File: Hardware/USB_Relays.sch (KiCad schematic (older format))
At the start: 0 parts

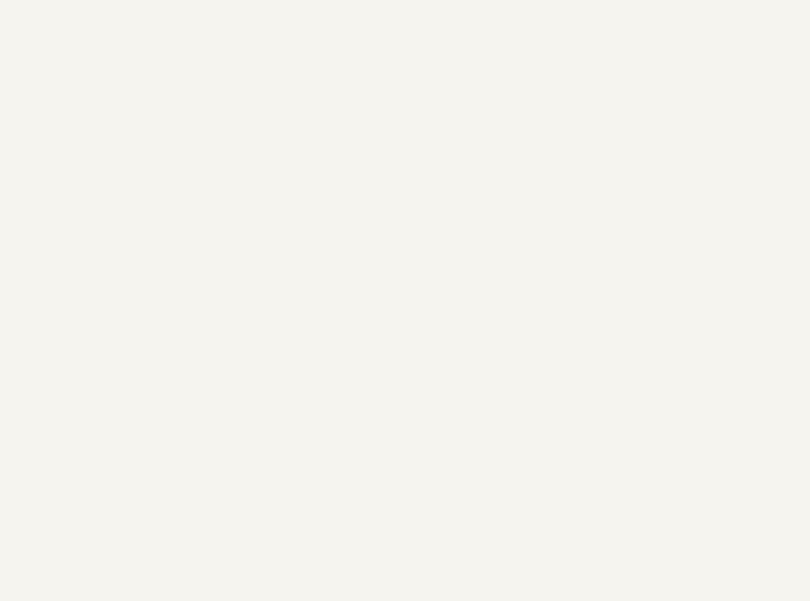
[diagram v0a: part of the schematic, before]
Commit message: [Hardware] Added terminal 3D models.
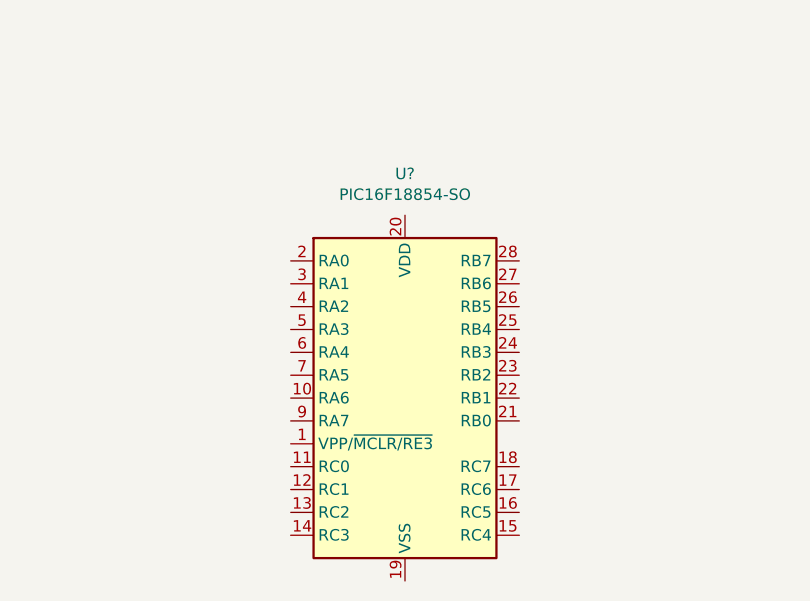
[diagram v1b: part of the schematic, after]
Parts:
- added U?: PIC16F18854-SO, Package_SO:SOIC-28W_7.5x17.9mm_P1.27mm, symbol MCU_Microchip_PIC16:PIC16F18854-SO
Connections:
- new net: U?.19 (VSS), U?.8 (VSS)
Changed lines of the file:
@@
 F1 "USB.sch" 50
 $EndSheet
+$Comp
+L MCU_Microchip_PIC16:PIC16F18854-SO U?
+U 1 1 6170521F
+P 3850 5250
+F 0 "U?" H 3850 6231 50  0000 C CNN
+F 1 "PIC16F18854-SO" H 3850 6140 50  0000 C CNN
+F 2 "Package_SO:SOIC-28W_7.5x17.9mm_P1.27mm" H 3850 4150 50  0001 C CNN
+F 3 "http://ww1.microchip.com/downloads/en/DeviceDoc/PIC16(L)F18854%20Data%20Sheet_DS40001826C.pdf" H 4150 4650 50  0001 C CNN
+	1    3850 5250
+	1    0    0    -1
+$EndComp
 $EndSCHEMATC

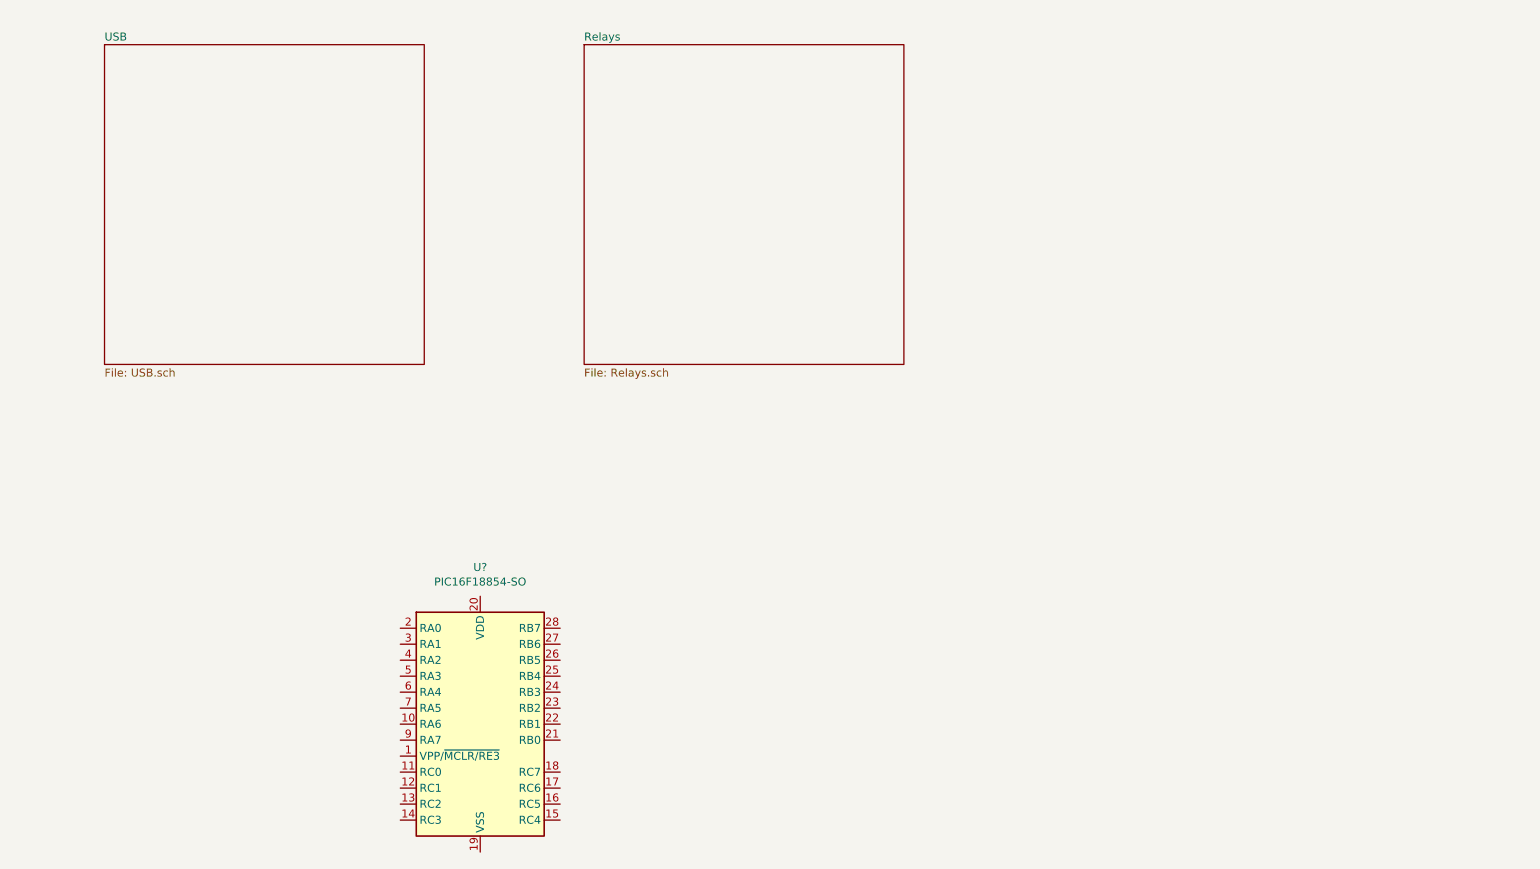
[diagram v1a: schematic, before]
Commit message: [Hardware] Added microcontroller-related schematic.
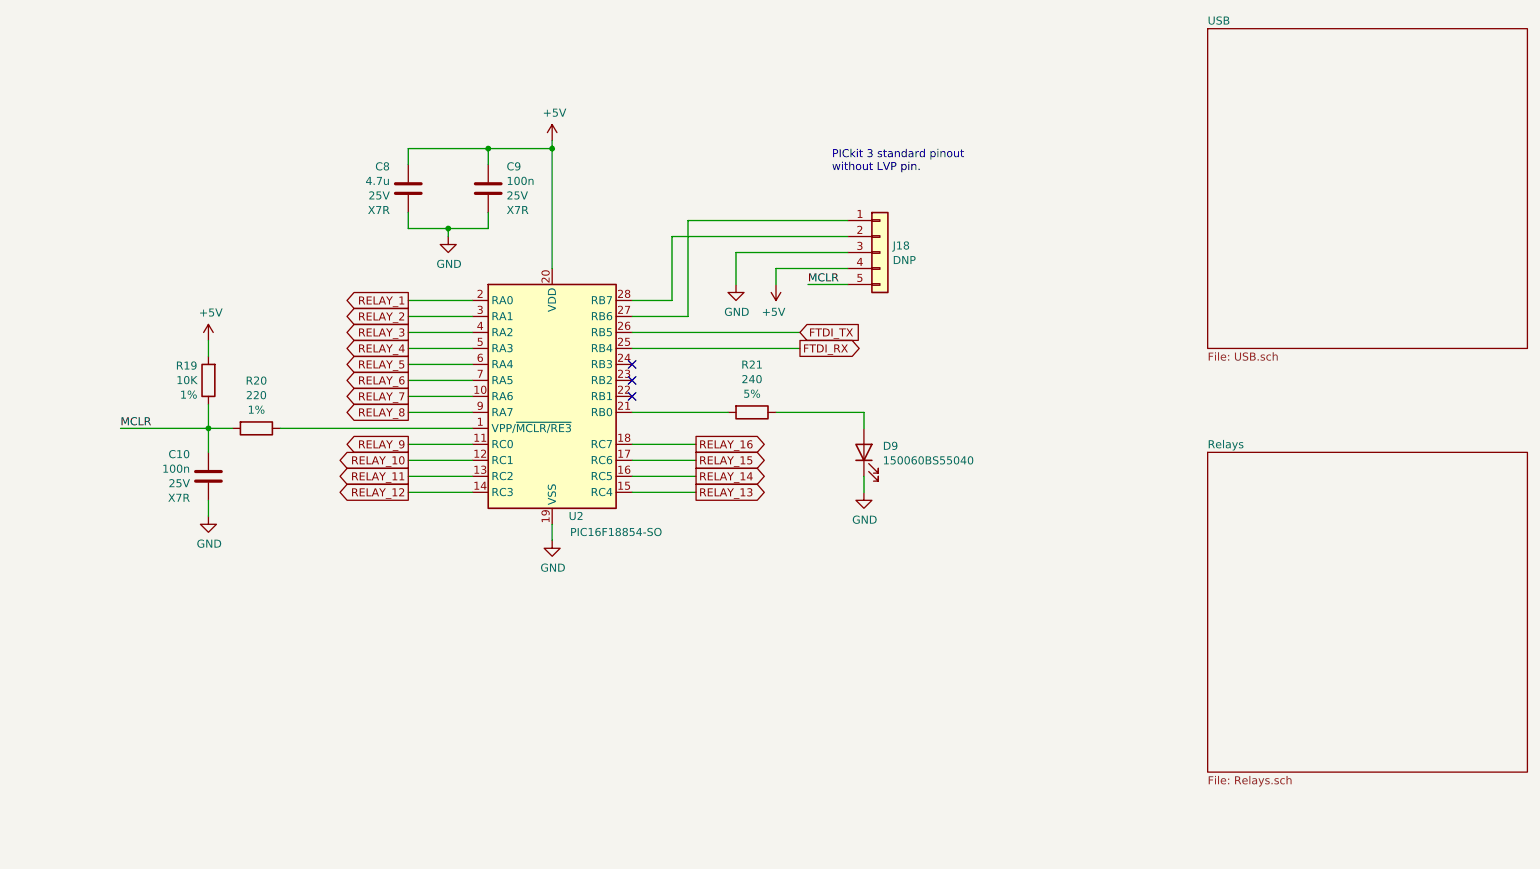
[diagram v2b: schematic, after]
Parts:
- added C10, C9: 100n, Capacitor_SMD:C_0603_1608Metric_Pad1.08x0.95mm_HandSolder, symbol Device:C
- added C8: 4.7u, Capacitor_SMD:C_0805_2012Metric_Pad1.18x1.45mm_HandSolder, symbol Device:C
- added D9: 150060BS55040, LED_SMD:LED_0201_0603Metric_Pad0.64x0.40mm_HandSolder, symbol Device:LED
- added J18: DNP, Connector_PinHeader_2.54mm:PinHeader_1x05_P2.54mm_Vertical, symbol Connector_Generic:Conn_01x05
- added R19: 10K, Resistor_SMD:R_0603_1608Metric_Pad0.98x0.95mm_HandSolder, symbol Device:R
- added R20: 220, Resistor_SMD:R_0603_1608Metric_Pad0.98x0.95mm_HandSolder, symbol Device:R
- added R21: 240, Resistor_SMD:R_1206_3216Metric_Pad1.30x1.75mm_HandSolder, symbol Device:R
- gave numbers to parts that had none: 1
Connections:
- net at U2.1 (VPP/~MCLR/RE3): now also R20.1
- net RELAY_7: now reaches U2.10 (RA6)
- net RELAY_9: now reaches U2.11 (RC0)
- net RELAY_10: now reaches U2.12 (RC1)
- net RELAY_11: now reaches U2.13 (RC2)
- net RELAY_12: now reaches U2.14 (RC3)
- net RELAY_13: now reaches U2.15 (RC4)
- net RELAY_14: now reaches U2.16 (RC5)
- net RELAY_15: now reaches U2.17 (RC6)
- net RELAY_16: now reaches U2.18 (RC7)
- net GND: now reaches U2.19 (VSS), U2.8 (VSS)
- net GND: now also C10.2, C8.2, C9.2, D9.1 (K), J18.3 (Pin_3)
- net RELAY_1: now reaches U2.2 (RA0)
- net +5V: now reaches U2.20 (VDD)
- net +5V: now also C8.1, C9.1, J18.4 (Pin_4), R19.2
- net at U2.21 (RB0): now also R21.2
- net FTDI_RX: now reaches U2.25 (RB4)
- net FTDI_TX: now reaches U2.26 (RB5)
- net at U2.27 (RB6): now also J18.1 (Pin_1)
- net at U2.28 (RB7): now also J18.2 (Pin_2)
- net RELAY_2: now reaches U2.3 (RA1)
- net RELAY_3: now reaches U2.4 (RA2)
- net RELAY_4: now reaches U2.5 (RA3)
- net RELAY_5: now reaches U2.6 (RA4)
- net RELAY_6: now reaches U2.7 (RA5)
- net RELAY_8: now reaches U2.9 (RA7)
- new net: D9.2 (A), R21.1
- new net MCLR: C10.1, J18.5 (Pin_5), R19.1, R20.2
- no-connect marks 0 -> 3
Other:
- note added: "PICkit 3 standard pinout\nwithout LVP pin."
- moved on the sheet: U2

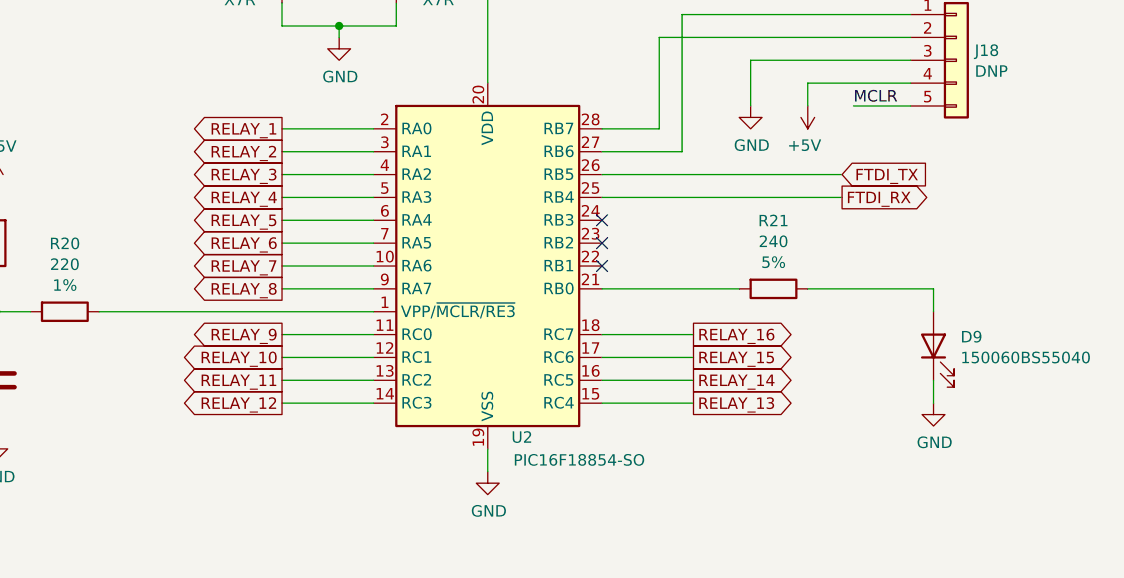
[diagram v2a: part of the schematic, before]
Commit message: [Hardware] Positioned components on PCB.
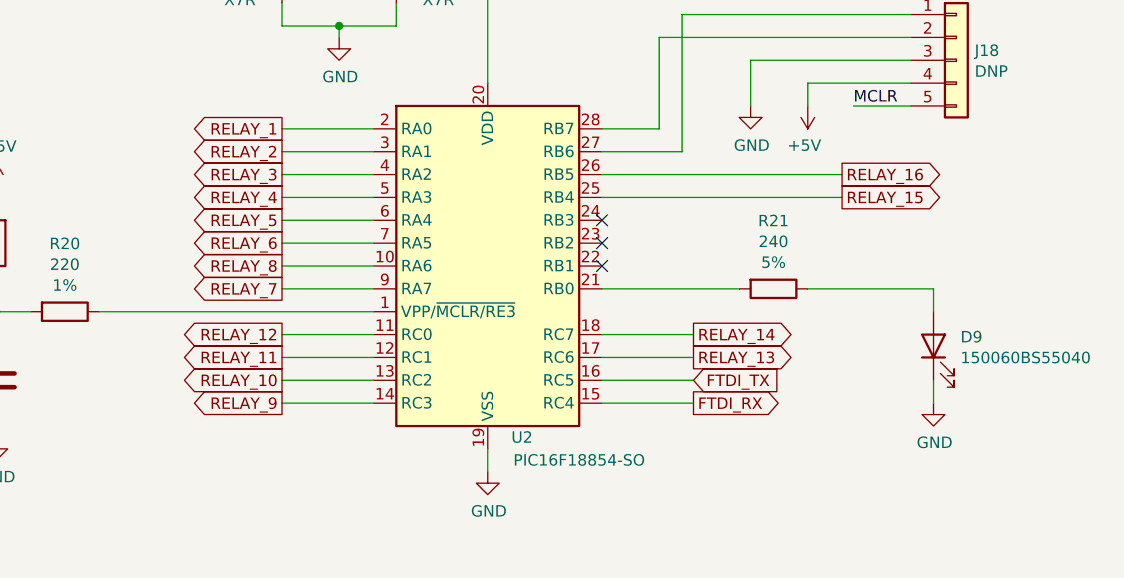
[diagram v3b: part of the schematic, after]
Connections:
- net FTDI_RX: now also U2.15 (RC4); no longer U2.25 (RB4)
- net FTDI_TX: now also U2.16 (RC5); no longer U2.26 (RB5)
- net RELAY_10: now also U2.13 (RC2); no longer U2.12 (RC1)
- net RELAY_11: now also U2.12 (RC1); no longer U2.13 (RC2)
- net RELAY_12: now also U2.11 (RC0); no longer U2.14 (RC3)
- net RELAY_13: now also U2.17 (RC6); no longer U2.15 (RC4)
- net RELAY_14: now also U2.18 (RC7); no longer U2.16 (RC5)
- net RELAY_15: now also U2.25 (RB4); no longer U2.17 (RC6)
- net RELAY_16: now also U2.26 (RB5); no longer U2.18 (RC7)
- net RELAY_7: now also U2.9 (RA7); no longer U2.10 (RA6)
- net RELAY_8: now also U2.10 (RA6); no longer U2.9 (RA7)
- net RELAY_9: now also U2.14 (RC3); no longer U2.11 (RC0)
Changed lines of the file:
@@
 Wire Wire Line
 	2150 3400 2300 3400
-Text GLabel 5850 2800 2    50   Input ~ 0
+Text GLabel 5200 3700 2    50   Input ~ 0
 FTDI_TX
-Text GLabel 5850 2900 2    50   Output ~ 0
+Text GLabel 5200 3800 2    50   Output ~ 0
 FTDI_RX
 Wire Wire Line
@@
 Text GLabel 3400 3100 0    50   Output ~ 0
 RELAY_6
+Text GLabel 3400 3300 0    50   Output ~ 0
+RELAY_7
 Text GLabel 3400 3200 0    50   Output ~ 0
-RELAY_7
-Text GLabel 3400 3300 0    50   Output ~ 0
 RELAY_8
 Wire Wire Line
@@
 Wire Wire Line
 	3400 3300 3800 3300
+Text GLabel 3400 3800 0    50   Output ~ 0
+RELAY_9
+Text GLabel 3400 3700 0    50   Output ~ 0
+RELAY_10
+Text GLabel 3400 3600 0    50   Output ~ 0
+RELAY_11
 Text GLabel 3400 3500 0    50   Output ~ 0
-RELAY_9
-Text GLabel 3400 3600 0    50   Output ~ 0
-RELAY_10
-Text GLabel 3400 3700 0    50   Output ~ 0
-RELAY_11
-Text GLabel 3400 3800 0    50   Output ~ 0
 RELAY_12
 Wire Wire Line
@@
 Wire Wire Line
 	3800 3800 3400 3800
-Text GLabel 5200 3800 2    50   Output ~ 0
+Text GLabel 5200 3600 2    50   Output ~ 0
 RELAY_13
-Text GLabel 5200 3700 2    50   Output ~ 0
+Text GLabel 5200 3500 2    50   Output ~ 0
 RELAY_14
-Text GLabel 5200 3600 2    50   Output ~ 0
+Text GLabel 5850 2900 2    50   Output ~ 0
 RELAY_15
-Text GLabel 5200 3500 2    50   Output ~ 0
+Text GLabel 5850 2800 2    50   Output ~ 0
 RELAY_16
 Wire Wire Line
